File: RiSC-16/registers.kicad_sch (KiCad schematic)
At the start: 0 parts

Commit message: First draft of register file.
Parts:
- added C10, C6, C7, C8, C9: 0.1 uF, symbol Device:C_Small_US
- added U10: 74LS00, symbol 74xx:74LS00
- added U6, U7: 74LS670, symbol 74xx:74LS670
- added U8, U9: 74LS257, symbol 74xx:74LS257
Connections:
- new net: U10.10, U10.6
- new net: U10.8, U7.12 (~{Ew})
- new net: U6.6 (Q4), U8.10 (I1d), U9.10 (I1d)
- new net: U7.6 (Q4), U8.11 (I0d), U9.11 (I0d)
- new net: U6.7 (Q3), U8.13 (I1c), U9.13 (I1c)
- new net: U7.7 (Q3), U8.14 (I0c), U9.14 (I0c)
- new net: U7.10 (Q1), U8.2 (I0a), U9.2 (I0a)
- new net: U6.10 (Q1), U8.3 (I1a), U9.3 (I1a)
- new net: U7.9 (Q2), U8.5 (I0b), U9.5 (I0b)
- new net: U6.9 (Q2), U8.6 (I1b), U9.6 (I1b)
- new net: U10.3, U6.12 (~{Ew})
- new net +5V: C10.1, C6.1, C7.1, C8.1, C9.1, U10.14 (VCC), U6.16 (VCC), U7.16 (VCC), U8.16 (VCC), U9.16 (VCC)
- new net GND: C10.2, C6.2, C7.2, C8.2, C9.2, U10.12, U10.13, U10.7 (GND), U6.11 (~{Er}), U6.8 (GND), U7.11 (~{Er}), U7.8 (GND), U8.8 (GND), U9.8 (GND)
- new net RAout: U8.15 (OE)
- new net RDout: U9.15 (OE)
- new net RWin: U10.2, U10.9
- new net a0: U8.4 (Za)
- new net a1: U8.7 (Zb)
- new net a2: U8.12 (Zc)
- new net a3: U8.9 (Zd)
- new net d0: U6.15 (D1), U7.15 (D1), U9.4 (Za)
- new net d1: U6.1 (D2), U7.1 (D2), U9.7 (Zb)
- new net d2: U6.2 (D3), U7.2 (D3), U9.12 (Zc)
- new net d3: U6.3 (D4), U7.3 (D4), U9.9 (Zd)
- new net ra0: U6.5 (Ra), U7.5 (Ra)
- new net ra1: U6.4 (Rb), U7.4 (Rb)
- new net ra2: U8.1 (S), U9.1 (S)
- new net wa0: U6.14 (Wa), U7.14 (Wa)
- new net wa1: U6.13 (Wb), U7.13 (Wb)
- new net wa2: U10.1, U10.4, U10.5
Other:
- note added: "Place decoupling capacitors near each IC."
- note added: "R0 to R3"
- note added: "R4 to R7"
- note added: "Register file 4 bit slice Four required for complete file."

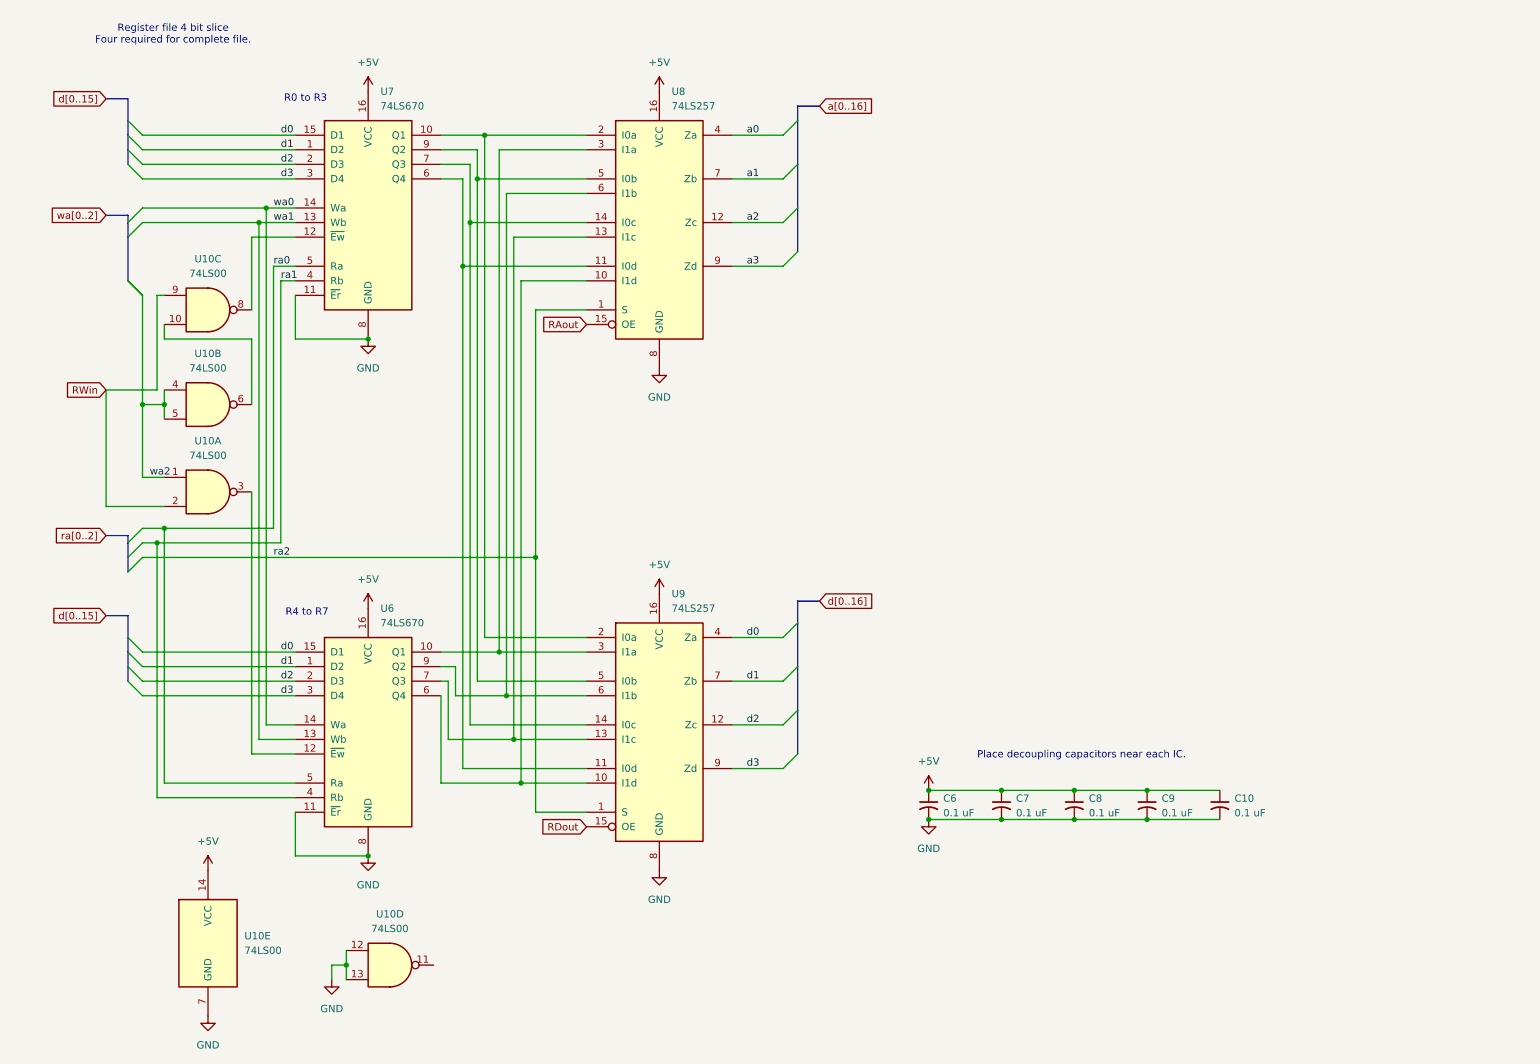
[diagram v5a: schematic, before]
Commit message: Added a custom symbol for the AM29705. Reworked to use it in two different approaches.
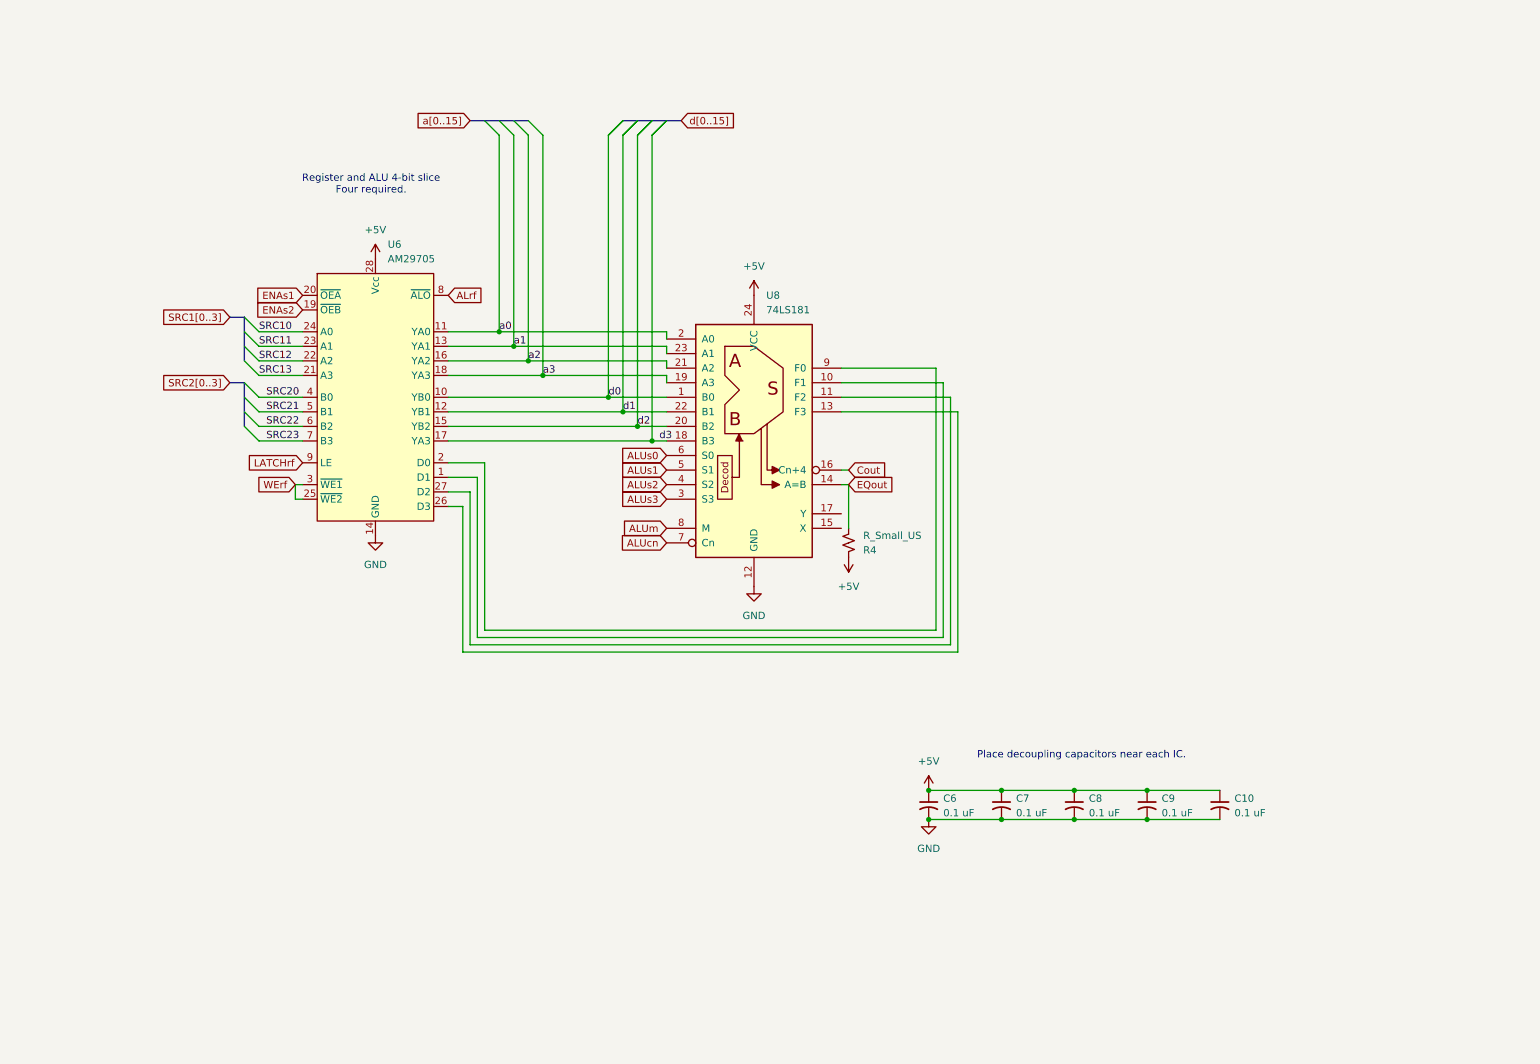
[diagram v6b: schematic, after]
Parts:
- removed U10: 74LS00, symbol 74xx:74LS00
- removed U6, U7: 74LS670, symbol 74xx:74LS670
- removed U8, U9: 74LS257, symbol 74xx:74LS257
- added R4: R_Small_US, symbol Device:R_Small_US
- added U6: AM29705, symbol AMD Bit Slice:AM29705_Register_File
- added U8: 74LS181, symbol 74xx:74LS181
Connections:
- net +5V: now also R4.1, U6.28 (Vcc), U8.24 (VCC)
- net GND: now also U6.14 (GND), U8.12 (GND)
- net a0: now also U6.11 (YA0), U8.2 (A0)
- net a1: now also U6.13 (YA1), U8.23 (A1)
- net a2: now also U6.16 (YA2), U8.21 (A2)
- net a3: now also U6.18 (YA3), U8.19 (A3)
- net d0: now also U6.10 (YB0), U8.1 (B0)
- net d1: now also U6.12 (YB1), U8.22 (B1)
- net d2: now also U6.15 (YB2), U8.20 (B2)
- net d3: now also U6.17 (YA3), U8.18 (B3)
- new net: U6.1 (D1), U8.10 (F1)
- new net: U6.27 (D2), U8.11 (F2)
- new net: U6.26 (D3), U8.13 (F3)
- new net: U6.2 (D0), U8.9 (F0)
- new net ALUcn: U8.7 (Cn)
- new net ALUm: U8.8 (M)
- new net ALUs0: U8.6 (S0)
- new net ALUs1: U8.5 (S1)
- new net ALUs2: U8.4 (S2)
- new net ALUs3: U8.3 (S3)
- new net ALrf: U6.8 (~{ALO})
- new net Cout: U8.16 (Cn+4)
- new net ENAs1: U6.20 (~{OEA})
- new net ENAs2: U6.19 (~{OEB})
- new net EQout: R4.2, U8.14 (A=B)
- new net LATCHrf: U6.9 (LE)
- new net SRC10: U6.24 (A0)
- new net SRC11: U6.23 (A1)
- new net SRC12: U6.22 (A2)
- new net SRC13: U6.21 (A3)
- new net SRC20: U6.4 (B0)
- new net SRC21: U6.5 (B1)
- new net SRC22: U6.6 (B2)
- new net SRC23: U6.7 (B3)
- new net WErf: U6.25 (~{WE2}), U6.3 (~{WE1})
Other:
- note added: "Register and ALU 4-bit slice Four required."
- note removed: "R0 to R3"
- note removed: "R4 to R7"
- note removed: "Register file 4 bit slice Four required for complete file."

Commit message: Check point of design.
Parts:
- removed R4: R_Small_US, symbol Device:R_Small_US
- removed U6: AM29705, symbol AMD Bit Slice:AM29705_Register_File
- added C11, C12, C13: 0.1 uF, symbol Device:C_Small_US
- added R2: R_Small_US, symbol Device:R_Small_US
- added U10, U11, U12, U13: AM29705, symbol AMD Bit Slice:AM29705_Register_File
- added U6, U7, U9: 74LS181, symbol 74xx:74LS181
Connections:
- net +5V: now also C11.1, C12.1, C13.1, R2.2, U10.28 (Vcc), U11.28 (Vcc), U12.28 (Vcc), U13.28 (Vcc), U6.24 (VCC), U7.24 (VCC), U9.24 (VCC)
- net ALUm: now also U6.8 (M), U7.8 (M), U9.8 (M)
- net ALUs0: now also U6.6 (S0), U7.6 (S0), U9.6 (S0)
- net ALUs1: now also U6.5 (S1), U7.5 (S1), U9.5 (S1)
- net ALUs2: now also U6.4 (S2), U7.4 (S2), U9.4 (S2)
- net ALUs3: now also U6.3 (S3), U7.3 (S3), U9.3 (S3)
- net ENAs1: now also U10.20 (~{OEA}), U11.20 (~{OEA}), U12.20 (~{OEA}), U13.20 (~{OEA})
- net ENAs2: now also U10.19 (~{OEB}), U11.19 (~{OEB}), U12.19 (~{OEB}), U13.19 (~{OEB})
- net GND: now also C11.2, C12.2, C13.2, U10.14 (GND), U11.14 (GND), U12.14 (GND), U13.14 (GND), U6.12 (GND), U7.12 (GND), U9.12 (GND)
- net LATCHrf: now also U10.9 (LE), U11.9 (LE), U12.9 (LE), U13.9 (LE)
- net SRC10: now also U10.24 (A0), U11.24 (A0), U12.24 (A0), U13.24 (A0)
- net SRC11: now also U10.23 (A1), U11.23 (A1), U12.23 (A1), U13.23 (A1)
- net SRC12: now also U10.22 (A2), U11.22 (A2), U12.22 (A2), U13.22 (A2)
- net SRC13: now also U12.21 (A3), U13.21 (A3)
- net SRC20: now also U10.4 (B0), U11.4 (B0), U12.4 (B0), U13.4 (B0)
- net SRC21: now also U10.5 (B1), U11.5 (B1), U12.5 (B1), U13.5 (B1)
- net SRC22: now also U10.6 (B2), U11.6 (B2), U12.6 (B2), U13.6 (B2)
- net SRC23: now also U10.7 (B3), U11.7 (B3), U12.7 (B3), U13.7 (B3)
- net WErf: now also U10.25 (~{WE2}), U10.3 (~{WE1}), U11.25 (~{WE2}), U11.3 (~{WE1}), U12.25 (~{WE2}), U12.3 (~{WE1}), U13.25 (~{WE2}), U13.3 (~{WE1})
- net a0: now also U10.11 (YA0), U6.2 (A0); no longer U8.2 (A0)
- net a1: now also U10.13 (YA1), U6.23 (A1); no longer U8.23 (A1)
- net a2: now also U10.16 (YA2), U6.21 (A2); no longer U8.21 (A2)
- net a3: now also U10.18 (YA3), U6.19 (A3); no longer U8.19 (A3)
- net d0: now also U10.10 (YB0), U6.1 (B0); no longer U8.1 (B0)
- net d1: now also U10.12 (YB1), U6.22 (B1); no longer U8.22 (B1)
- net d2: now also U10.15 (YB2), U6.20 (B2); no longer U8.20 (B2)
- net d3: now also U10.17 (YB3), U6.18 (B3); no longer U8.18 (B3)
- net at U8.10 (F1): now also U12.1 (D1)
- net at U8.11 (F2): now also U12.27 (D2)
- net at U8.13 (F3): now also U12.26 (D3)
- net at U8.9 (F0): now also U12.2 (D0)
- net ALUcn: no longer names the net of U8.7 (Cn)
- net ALUcn: now also U7.16 (Cn+4)
- net Cout: no longer names the net of U8.16 (Cn+4)
- net Cout: now also U9.7 (Cn)
- net EQout renamed ALUeq
- net ALUeq: now also R2.1, U6.14 (A=B), U7.14 (A=B), U9.14 (A=B)
- new net: U11.1 (D1), U7.10 (F1)
- new net: U11.2 (D0), U7.9 (F0)
- new net: U11.26 (D3), U7.13 (F3)
- new net: U11.27 (D2), U7.11 (F2)
- new net: U6.16 (Cn+4), U7.7 (Cn)
- new net: U13.1 (D1), U9.10 (F1)
- new net: U13.27 (D2), U9.11 (F2)
- new net: U13.26 (D3), U9.13 (F3)
- new net: U13.2 (D0), U9.9 (F0)
- new net: U10.1 (D1), U6.10 (F1)
- new net: U10.2 (D0), U6.9 (F0)
- new net: U10.26 (D3), U6.13 (F3)
- new net: U10.27 (D2), U6.11 (F2)
- new net AL0: U10.8 (~{ALO}), U11.8 (~{ALO}), U12.8 (~{ALO}), U13.8 (~{ALO})
- new net ALUcin: U6.7 (Cn)
- new net ALUcout: U9.16 (Cn+4)
- new net a10: U12.16 (YA2), U8.21 (A2)
- new net a11: U12.18 (YA3), U8.19 (A3)
- new net a12: U13.11 (YA0), U9.2 (A0)
- new net a13: U13.13 (YA1), U9.23 (A1)
- new net a14: U13.16 (YA2), U9.21 (A2)
- new net a15: U13.18 (YA3), U9.19 (A3)
- new net a4: U11.11 (YA0), U7.2 (A0)
- new net a5: U11.13 (YA1), U7.23 (A1)
- new net a6: U11.16 (YA2), U7.21 (A2)
- new net a7: U11.18 (YA3), U7.19 (A3)
- new net a8: U12.11 (YA0), U8.2 (A0)
- new net a9: U12.13 (YA1), U8.23 (A1)
- new net d10: U12.15 (YB2), U8.20 (B2)
- new net d11: U12.17 (YB3), U8.18 (B3)
- new net d12: U13.10 (YB0), U9.1 (B0)
- new net d13: U13.12 (YB1), U9.22 (B1)
- new net d14: U13.15 (YB2), U9.20 (B2)
- new net d15: U13.17 (YB3), U9.18 (B3)
- new net d4: U11.10 (YB0), U7.1 (B0)
- new net d5: U11.12 (YB1), U7.22 (B1)
- new net d6: U11.15 (YB2), U7.20 (B2)
- new net d7: U11.17 (YB3), U7.18 (B3)
- new net d8: U12.10 (YB0), U8.1 (B0)
- new net d9: U12.12 (YB1), U8.22 (B1)
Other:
- note removed: "Register and ALU 4-bit slice Four required."
- moved on the sheet: C10, C6, C7, C8, C9

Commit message: Moved and renamed pages.
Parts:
- removed C10, C11, C12, C13, C6, C7, C8, C9: 0.1 uF, symbol Device:C_Small_US
- removed R2: R_Small_US, symbol Device:R_Small_US
- removed U10, U11, U12, U13: AM29705, symbol AMD Bit Slice:AM29705_Register_File
- removed U6, U7, U8, U9: 74LS181, symbol 74xx:74LS181
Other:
- note removed: "Place decoupling capacitors near each IC."
